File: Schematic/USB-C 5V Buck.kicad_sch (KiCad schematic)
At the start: 17 parts, among them Q25 CSD19531Q5A, Q26 CSD19531Q5A, U12 LM5148RGYR

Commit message: added sensors?
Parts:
- removed C110: 2u2, symbol Device:C
- removed L2: 1u, symbol Device:L
- removed R125: 9k53, symbol Device:R
- removed R126: 40k2, symbol Device:R
- removed R127: 4k64, symbol Device:R
- removed R128: 24k3, symbol Device:R
- removed R129: 100k, symbol Device:R
- removed R130: 9m, symbol Device:R
- removed U12: LM5148RGYR, LM5148RGYR:QFN50P550X350X100-25N, symbol LM5148RGYR:LM5148RGYR
- added C107, C108, C109, C110: 56u, symbol Device:C_Polarized
- added C117: 1u, symbol Device:C
- added C118: 100n, symbol Device:C
- added C119: 100p, symbol Device:C
- added C120: 2u2, symbol Device:C
- added C121, C125: 220n, symbol Device:C
- added C122, C123, C124: 47u, symbol Device:C
- added L1: 5u6, symbol Device:L
- added NT2: NetTie_2, symbol Device:NetTie_2
- added R108: 11k8, symbol Device:R
- added R109: 59k, symbol Device:R
- added R110: 100k, symbol Device:R
- added R111: 2k21, symbol Device:R
- added R112: 49R9, symbol Device:R
- added R113: 7m, symbol Device:R
- added U11: LM25190RGYR, RGY0019C-MFG, symbol LM25190RGYR:LM25190RGYR
- C111: value 820p -> 220n
- C112: value 30p -> 220n
- C113: value 100n -> 4n7
- C114: value 2u2 -> 68n
- C115: value 100n -> 47p
- C116: value 22u -> 1n
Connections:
- net GND: now also C111.2, C112.2, C107.2, C108.2, C109.2, C110.2, C117.1, C120.2, C121.2, C122.2, C123.2, C124.2, C125.2, NT2.2, U11.20 (EP), U11.8 (PGND); no longer C111.1, C112.1, C113.2, C114.2, C116.1
- net P5V0: now also C122.1, C123.1, C124.1, C125.1, R113.2; no longer C116.2
- net PACK+: now also C111.1, C112.1, C107.1, C108.1, C109.1, C110.1, U11.10 (VIN), U11.17 (EN)
- net VCC: now also C120.1, C121.1, R110.1, U11.16 (FPWM_SYNC), U11.7 (VCC); no longer C114.1
- net at Q25.1 (S), Q25.2 (S), Q25.3 (S)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: now also C118.2, L1.1, U11.12 (SW); no longer C115.1
- net at C115.2: now also R111.2, U11.3 (COMP)
- net at Q26.4 (G): now also U11.9 (LO)
- net at Q25.4 (G): now also U11.11 (HO)
- net VDDA renamed GNDA
- net GNDA: now also C114.1, C115.1, C116.1, NT2.1, R108.1, R109.1, U11.4 (FB), U11.5 (AGND)
- new net: C118.1, U11.13 (CBOOT)
- new net: C114.2, R111.1
- new net: C116.2, U11.1 (ISET)
- new net: L1.2, R112.2, R113.1
- new net: C117.2, U11.14 (BIAS)
- new net: R110.2, U11.15 (PG)
- new net: C119.2, R112.1, U11.18 (ISNS+)
- new net: C119.1, U11.19 (VOUT)
- new net: R109.2, U11.2 (RT)
- new net: C113.2, R108.2, U11.6 (IMON_ILIM)
- no-connect marks 5 -> 0
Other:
- note added: "5V, 6A Line"
- note added: "> 1W"
- note added: "P5V0 must support 3A(VBUS) + 0.315A(VCONN) = 3.315A with headroom, 5A is a good amount also some logic will require 5V: Optical Encoders, 10mA x 4: 40mA Other Sensors: idk, but prob < 1A 6A was the picked headroom"
- note added: "~13.7mΩ"
- note removed: "5V, 5A Line"
- note removed: "<=11mΩ"
- note removed: ">=1W"
- note removed: "P5V0 must support 3A(VBUS) + 0.315A(VCONN) = 3.315A with headroom, 5A is a good amount"

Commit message: 1st Schematic Review
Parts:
- renumbered C107 to C110, C108 to C111, C109 to C112, C110 to C113, C111 to C114, C112 to C115, C113 to C116, C114 to C117, C115 to C118, C116 to C119, C117 to C120, C118 to C121, C119 to C122, C120 to C123, C121 to C124, C122 to C125, C123 to C126, C124 to C127, C125 to C128, R108 to R110, R109 to R111, R110 to R112, R111 to R113, R112 to R114, R113 to R115, U11 to U14

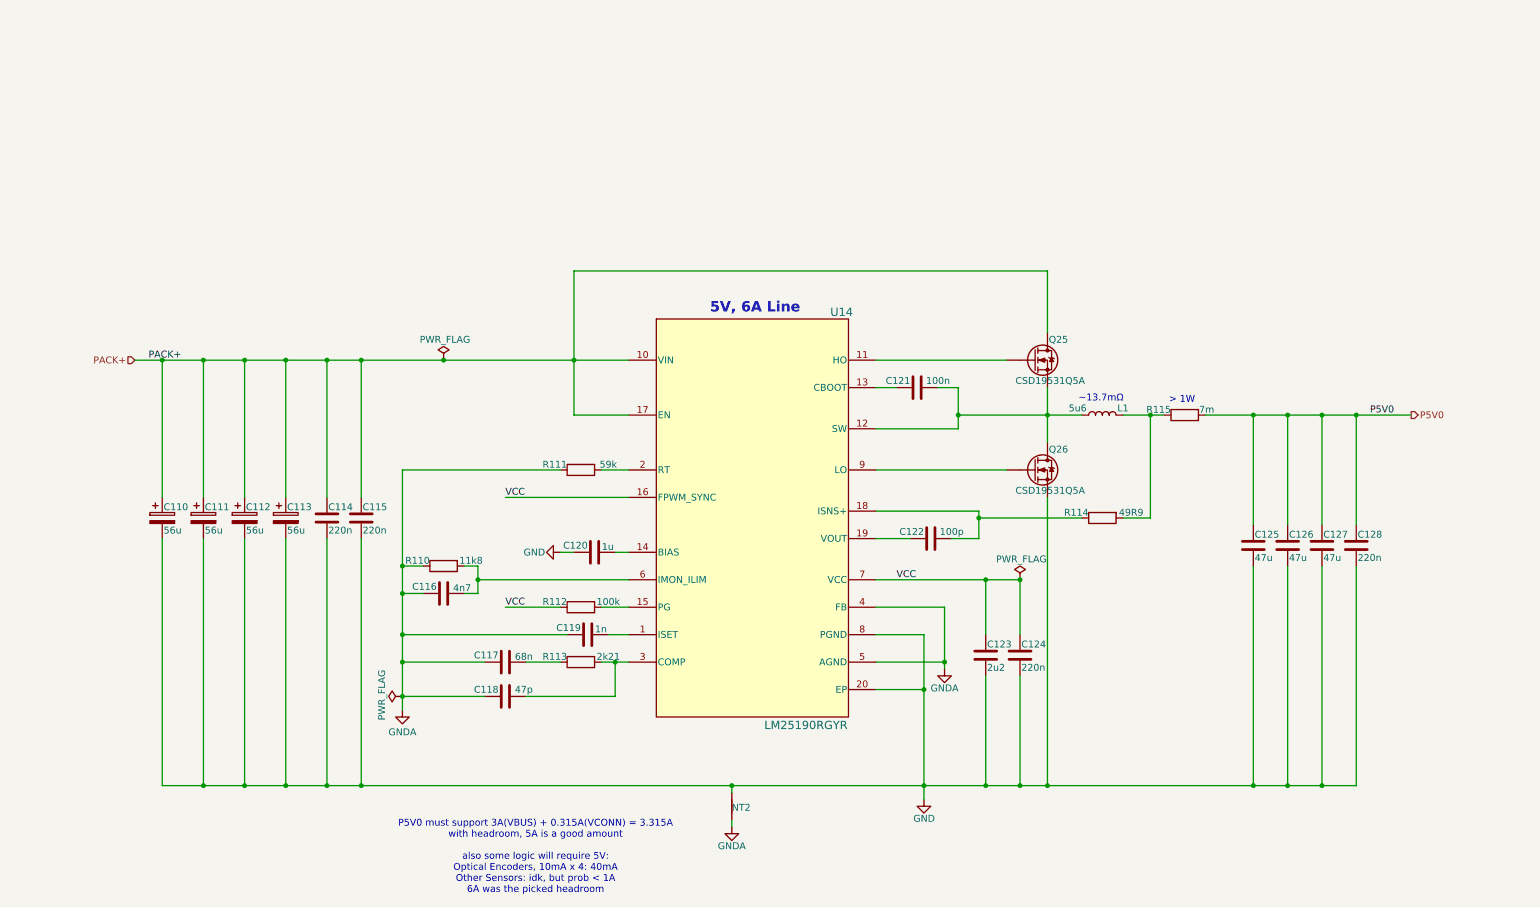
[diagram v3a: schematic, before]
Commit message: fixed power lines
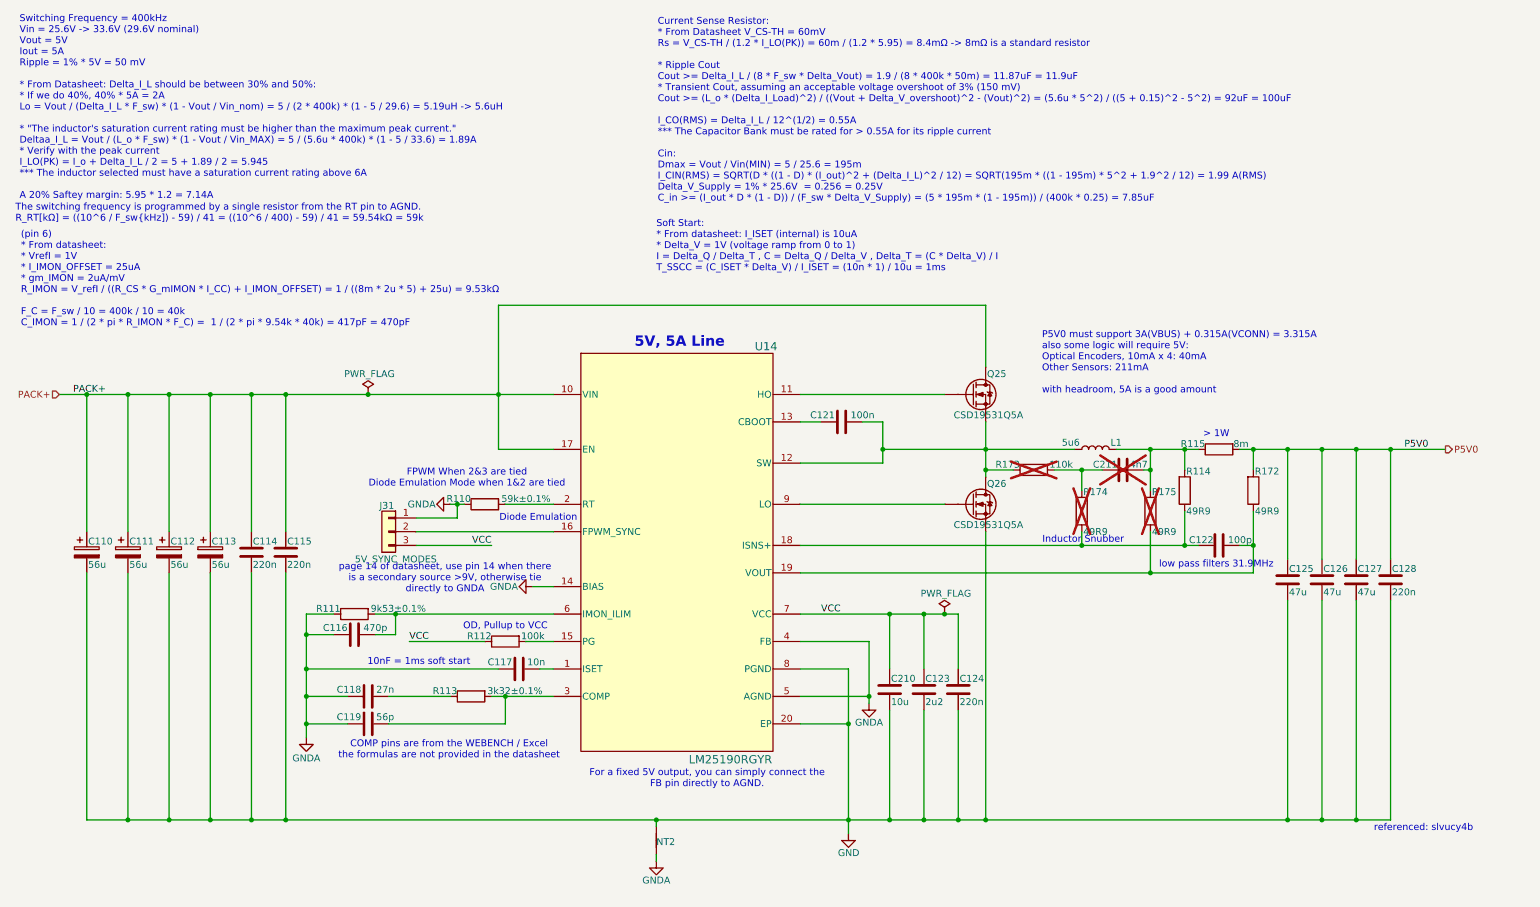
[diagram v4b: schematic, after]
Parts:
- removed C120: 1u, symbol Device:C
- added C210: 10u, symbol Device:C
- added C211: 4n7, symbol Device:C
- added J31: 5V_SYNC_MODES, symbol Connector_Generic:Conn_01x03
- added R172, R174, R175: 49R9, symbol Device:R
- added R173: 110k, symbol Device:R
- C116: value 4n7 -> 470p
- C117: value 68n -> 10n
- C118: value 47p -> 27n
- C119: value 1n -> 56p
- R110: value 11k8 -> 59k±0.1%
- R111: value 59k -> 9k53±0.1%
- R113: value 2k21 -> 3k32±0.1%
- R115: value 7m -> 8m
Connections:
- net GND: now also C210.2
- net GNDA: now also U14.14 (BIAS), J31.1 (Pin_1)
- net P5V0: now also R172.2
- net VCC: now also C210.1, J31.3 (Pin_3); no longer U14.16 (FPWM_SYNC)
- net at C121.2, L1.1, Q25.1 (S)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: now also R173.1
- net at C117.2: now also U14.1 (ISET); no longer R113.1
- net at C119.2: now also R113.2, U14.3 (COMP); no longer U14.1 (ISET)
- net at L1.2, R114.2, R115.1: now also C211.2, R175.2
- net at R114.1, U14.18 (ISNS+): now also C122.1, R174.1; no longer C122.2
- net at U14.19 (VOUT): now also C122.2, R172.1, R175.1; no longer C122.1
- net at U14.2 (RT): now also R110.2; no longer R111.2
- net at C116.2, U14.6 (IMON_ILIM): now also R111.2; no longer R110.2
- new net: J31.2 (Pin_2), U14.16 (FPWM_SYNC)
- new net: C118.2, R113.1
- new net: C211.1, R173.2, R174.2
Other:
- note added: "(pin 6) * From datasheet: * VrefI = 1V * I_IMON_OFFSET = 25uA * gm_IMON = 2uA/mV R_IMON = V_refI / ((R_CS * G_mIMON * I_CC) + I_IMON_OFFSET) = 1 / ((8m * 2u * 5) + 25u) = 9.53kΩ F_C = F_sw / 10 = 400k / 10 = 40k C_IMON = 1 / (2 * pi * R_IMON * F_C) = 1 / (2 * pi * 9.54k * 40k) = 417pF = 470pF"
- note added: "10nF = 1ms soft start"
- note added: "5V, 5A Line"
- note added: "COMP pins are from the WEBENCH / Excel the formulas are not provided in the datasheet"
- note added: "Current Sense Resistor: * From Datasheet V_CS-TH = 60mV Rs = V_CS-TH / (1.2 * I_LO(PK)) = 60m / (1.2 * 5.95) = 8.4mΩ -> 8mΩ is a standard resistor * Ripple Cout Cout >= Delta_I_L / (8 * F_sw * Delta_Vout) = 1.9 / (8 * 400k * 50m) = 11.87uF = 11.9uF * Transient Cout, assuming an acceptable voltage overshoot of 3% (150 mV) Cout >= (L_o * (Delta_I_Load)^2) / ((Vout + Delta_V_overshoot)^2 - (Vout)^2)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"
- note added: "Diode Emulation"
- note added: "FPWM When 2&3 are tied Diode Emulation Mode when 1&2 are tied"
- note added: "For a fixed 5V output, you can simply connect the FB pin directly to AGND."
- note added: "Inductor Snubber"
- note added: "OD, Pullup to VCC"
- note added: "P5V0 must support 3A(VBUS) + 0.315A(VCONN) = 3.315A also some logic will require 5V: Optical Encoders, 10mA x 4: 40mA Other Sensors: 211mA with headroom, 5A is a good amount"
- note added: "Soft Start: * From datasheet: I_ISET (internal) is 10uA * Delta_V = 1V (voltage ramp from 0 to 1) I = Delta_Q / Delta_T , C = Delta_Q / Delta_V , Delta_T = (C * Delta_V) / I T_SSCC = (C_ISET * Delta_V) / I_ISET = (10n * 1) / 10u = 1ms"
- note added: "Switching Frequency = 400kHz Vin = 25.6V -> 33.6V (29.6V nominal) Vout = 5V Iout = 5A Ripple = 1% * 5V = 50 mV * From Datasheet: Delta_I_L should be between 30% and 50%: * If we do 40%, 40% * 5A = 2A Lo = Vout / (Delta_I_L * F_sw) * (1 - Vout / Vin_nom) = 5 / (2 * 400k) * (1 - 5 / 29.6) = 5.19uH -> 5.6uH * "The inductor's saturation current rating must be higher than the maximum peak current." De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"
- note added: "The switching frequency is programmed by a single resistor from the RT pin to AGND. R_RT[kΩ] = ((10^6 / F_sw{kHz]) - 59) / 41 = ((10^6 / 400) - 59) / 41 = 59.54kΩ = 59k"
- note added: "low pass filters 31.9MHz"
- note added: "page 14 of datasheet, use pin 14 when there is a secondary source >9V, otherwise tie directly to GNDA"
- note added: "referenced: slvucy4b"
- note removed: "5V, 6A Line"
- note removed: "P5V0 must support 3A(VBUS) + 0.315A(VCONN) = 3.315A with headroom, 5A is a good amount also some logic will require 5V: Optical Encoders, 10mA x 4: 40mA Other Sensors: idk, but prob < 1A 6A was the picked headroom"
- note removed: "~13.7mΩ"
- moved on the sheet: C110, C111, C112, C113, C114, C115, C121, C123, C124, C125, C126, C127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

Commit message: updates
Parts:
- renumbered C118 to C117, C119 to C118, C117 to C119, C121 to C120, C210 to C121, C123 to C122, C124 to C123, C211 to C124, C122 to C125, C125 to C126, C126 to C127, C127 to C128, C128 to C129, J31 to J10, R111 to R115, R113 to R116, R110 to R117, R112 to R118, R173 to R119, R174 to R120, R175 to R121, R114 to R122, R115 to R123, R172 to R124
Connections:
- net GND: now also U14.14 (BIAS)
- net GNDA: no longer U14.14 (BIAS)
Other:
- note added: "page 14 of datasheet, use pin 14 when there is a secondary source >9V, otherwise tie directly to GND"
- note removed: "page 14 of datasheet, use pin 14 when there is a secondary source >9V, otherwise tie directly to GNDA"

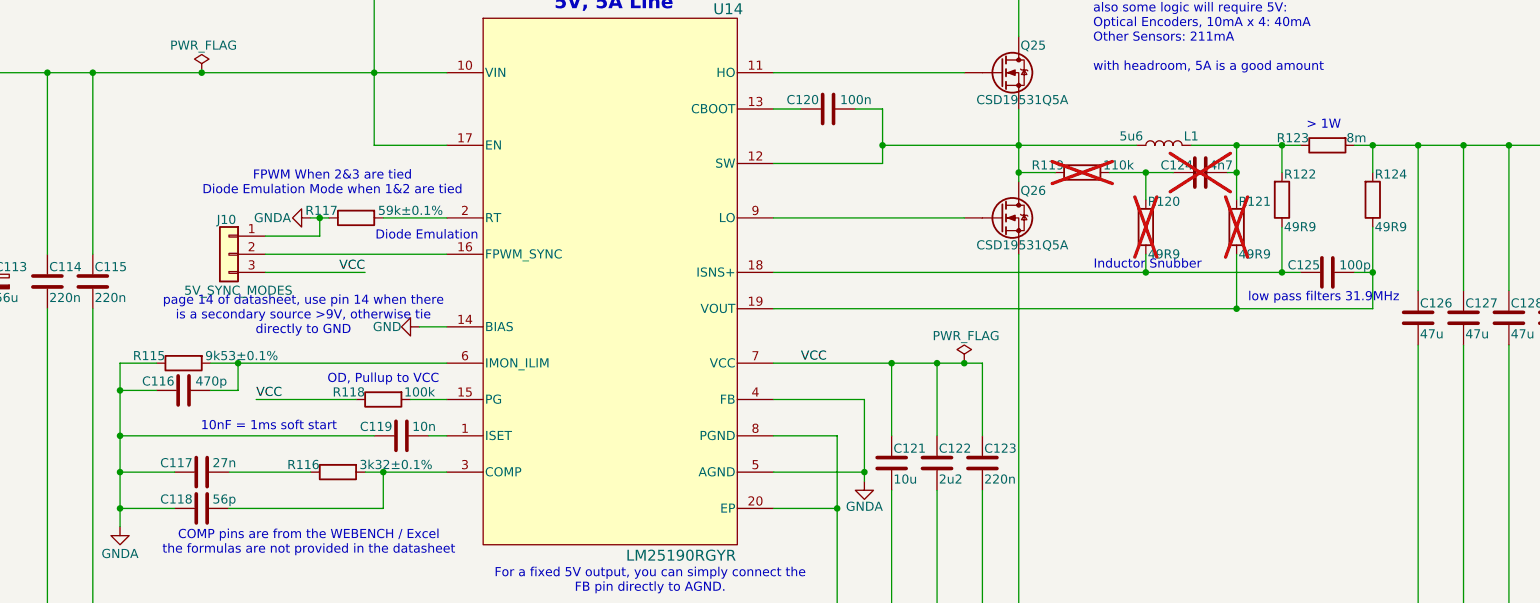
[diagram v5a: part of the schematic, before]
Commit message: updated fuel guage
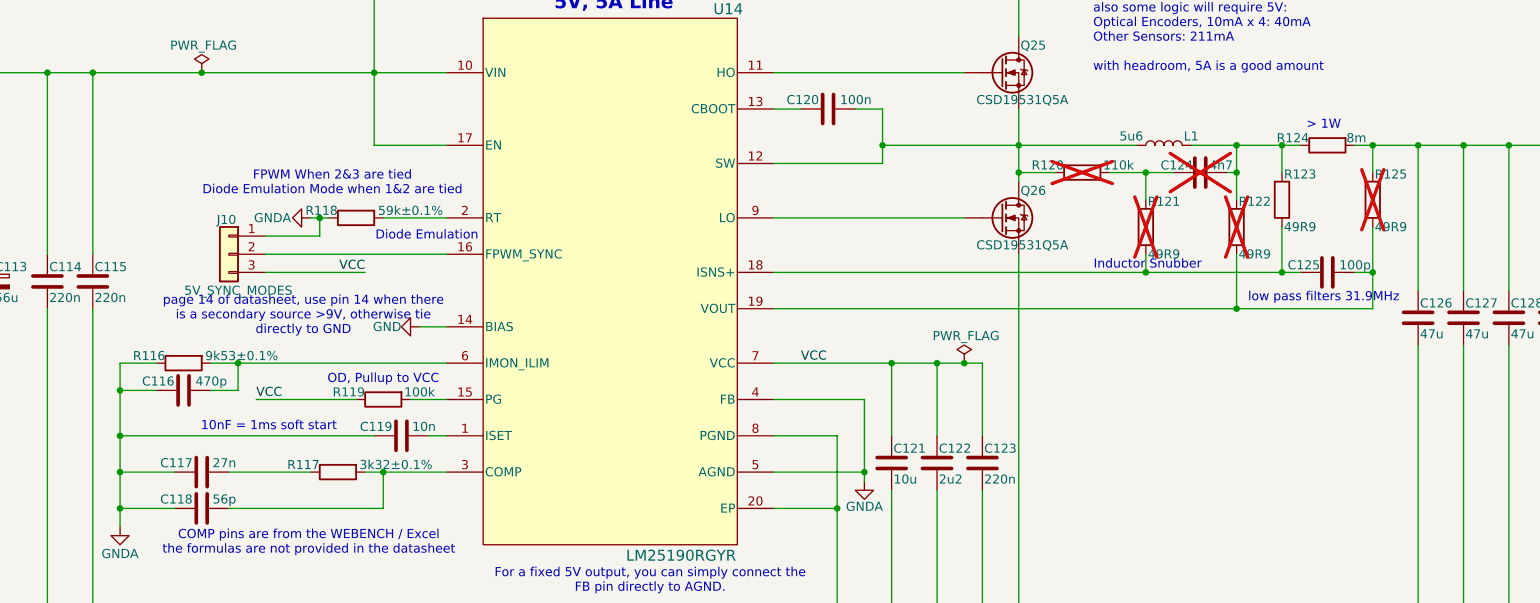
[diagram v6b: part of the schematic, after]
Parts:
- R125: renamed from R124; now not fitted
- renumbered R115 to R116, R116 to R117, R117 to R118, R118 to R119, R119 to R120, R120 to R121, R121 to R122, R122 to R123, R123 to R124
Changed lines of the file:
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@@
 		(on_board yes)
 		(dnp yes)
-		(property "Reference" "R121"
+		(property "Reference" "R122"
 			(at 226.06 103.124 0)
 			(effects
@@
 			(project "STAR"
 				(path "/fc8533bc-25dd-4c20-9b4c-ffebebd6739b/ec72a35b-e7f2-4422-8859-60e9fb848154/e37625a4-4166-4d08-b145-52540d65bd12"
-					(reference "R121")
+					(reference "R122")
 					(unit 1)
 				)
@@
 		(on_board yes)
 		(dnp no)
-		(property "Reference" "R118"
+		(property "Reference" "R119"
 			(at 99.314 129.794 90)
 			(effects
@@
 			(project "STAR"
 				(path "/fc8533bc-25dd-4c20-9b4c-ffebebd6739b/ec72a35b-e7f2-4422-8859-60e9fb848154/e37625a4-4166-4d08-b145-52540d65bd12"
-					(reference "R118")
+					(reference "R119")
 					(unit 1)
 				)
@@
 		(on_board yes)
 		(dnp no)
-		(property "Reference" "R122"
+		(property "Reference" "R123"
 			(at 232.41 99.314 0)
 			(effects
@@
 			(project "STAR"
 				(path "/fc8533bc-25dd-4c20-9b4c-ffebebd6739b/ec72a35b-e7f2-4422-8859-60e9fb848154/e37625a4-4166-4d08-b145-52540d65bd12"
-					(reference "R122")
+					(reference "R123")
 					(unit 1)
 				)
@@
 		(on_board yes)
 		(dnp no)
-		(property "Reference" "R115"
+		(property "Reference" "R116"
 			(at 71.374 124.714 90)
 			(effects
@@
 			(project "STAR"
 				(path "/fc8533bc-25dd-4c20-9b4c-ffebebd6739b/ec72a35b-e7f2-4422-8859-60e9fb848154/e37625a4-4166-4d08-b145-52540d65bd12"
-					(reference "R115")
+					(reference "R116")
 					(unit 1)
 				)
@@
 		(on_board yes)
 		(dnp yes)
-		(property "Reference" "R120"
+		(property "Reference" "R121"
 			(at 213.36 103.124 0)
 			(effects
@@
 			(project "STAR"
 				(path "/fc8533bc-25dd-4c20-9b4c-ffebebd6739b/ec72a35b-e7f2-4422-8859-60e9fb848154/e37625a4-4166-4d08-b145-52540d65bd12"
-					(reference "R120")
+					(reference "R121")
 					(unit 1)
 				)
@@
 		(on_board yes)
 		(dnp no)
-		(property "Reference" "R117"
+		(property "Reference" "R118"
 			(at 95.504 104.394 90)
 			(effects
@@
 			(project "STAR"
 				(path "/fc8533bc-25dd-4c20-9b4c-ffebebd6739b/ec72a35b-e7f2-4422-8859-60e9fb848154/e37625a4-4166-4d08-b145-52540d65bd12"
-					(reference "R117")
+					(reference "R118")
 					(unit 1)
 				)
@@
 		(in_bom yes)
 		(on_board yes)
-		(dnp no)
-		(property "Reference" "R124"
+		(dnp yes)
+		(property "Reference" "R125"
 			(at 245.11 99.314 0)
 			(effects
@@
 			(project "STAR"
 				(path "/fc8533bc-25dd-4c20-9b4c-ffebebd6739b/ec72a35b-e7f2-4422-8859-60e9fb848154/e37625a4-4166-4d08-b145-52540d65bd12"
-					(reference "R124")
+					(reference "R125")
 					(unit 1)
 				)
@@
 		(on_board yes)
 		(dnp yes)
-		(property "Reference" "R119"
+		(property "Reference" "R120"
 			(at 197.104 98.044 90)
 			(effects
@@
 			(project "STAR"
 				(path "/fc8533bc-25dd-4c20-9b4c-ffebebd6739b/ec72a35b-e7f2-4422-8859-60e9fb848154/e37625a4-4166-4d08-b145-52540d65bd12"
-					(reference "R119")
+					(reference "R120")
 					(unit 1)
 				)
@@
 		(on_board yes)
 		(dnp no)
-		(property "Reference" "R116"
+		(property "Reference" "R117"
 			(at 92.964 139.954 90)
 			(effects
@@
 			(project "STAR"
 				(path "/fc8533bc-25dd-4c20-9b4c-ffebebd6739b/ec72a35b-e7f2-4422-8859-60e9fb848154/e37625a4-4166-4d08-b145-52540d65bd12"
-					(reference "R116")
+					(reference "R117")
 					(unit 1)
 				)
@@
 		(on_board yes)
 		(dnp no)
-		(property "Reference" "R123"
+		(property "Reference" "R124"
 			(at 231.394 94.234 90)
 			(effects
@@
 			(project "STAR"
 				(path "/fc8533bc-25dd-4c20-9b4c-ffebebd6739b/ec72a35b-e7f2-4422-8859-60e9fb848154/e37625a4-4166-4d08-b145-52540d65bd12"
-					(reference "R123")
+					(reference "R124")
 					(unit 1)
 				)
